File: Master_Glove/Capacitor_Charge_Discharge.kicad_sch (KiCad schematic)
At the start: 0 parts

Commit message: Switch+555+SR
work in progress
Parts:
- added C1: 10u, symbol Device:C
- added R8: 68k, symbol Device:R
- added SW1: SW_Push, symbol Switch:SW_Push
- added U3: MIC1551YM5-TR, Package_TO_SOT_SMD:SOT-23-5, symbol Battery_Management:MCP73811T-435I-OT
- added U4: TC7WH02FU, symbol 74xGxx:74AUC2G02
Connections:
- new net: C1.1, R8.2, U3.5 (TRG)
- new net: SW1.2, U3.4 (TRG)
- new net: U4.5, U4.7
- new net +5V: SW1.1, U3.1 (VS), U4.8 (VCC)
- new net 1Hz: R8.1, U3.3 (OUT), U4.1
- new net GND: C1.2, U3.2 (GND), U4.4 (GND)
- new net Reset: U4.6
- new net SR_Output: U4.2, U4.3
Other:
- note added: "1Hz generator with pushbutton"
- note added: "Reset"
- note added: "Set"
- note added: "Set-Reset circuit"
- note added: "f = 1 / ( k1*R*C ) k1 = 1.44"

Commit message: work on discharge
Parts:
- added C2: 18nF, symbol Device:C
- added C3, C4: 100nF, symbol Device:C
- added R9: 1k, symbol Device:R
- added U5: 74LVC1G08, symbol 74xGxx:74LVC1G08
- added U6: 74AHC1G14, symbol 74xGxx:74AHC1G14
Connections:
- net +5V: now also C3.1, C4.1, U6.5 (VCC)
- net GND: now also C2.2, C3.2, C4.2, U6.3 (GND)
- new net: C2.1, R9.2, U6.2
- new net 40KHz: R9.1, U6.4
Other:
- note added: "Enable?"
- note added: "Exemple A retravailler..."
- note added: "Schmitt oscillator circuit"

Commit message: Working on emitter Circuit
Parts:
- removed U5: 74LVC1G08, symbol 74xGxx:74LVC1G08
- added C7: 100nF, symbol Device:C
- added U5: MIC1551YM5-TR, Package_TO_SOT_SMD:SOT-23-5, symbol Battery_Management:MCP73811T-435I-OT
- added U7: TC7WH02FU, symbol 74xGxx:74AUC2G02
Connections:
- net +5V: now also C7.1, U7.8 (VCC)
- net 40KHz: now also U7.2
- net GND: now also C7.2, U7.4 (GND)
- net SR-_Output: now reaches U4.5, U4.7
- net SR-_Output: now also U7.1
- new net 555_En_pin: U7.7
- no-connect marks 0 -> 3
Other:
- note added: "555 circuit connected to sensor"
- note removed: "Enable?"
- note removed: "Exemple A retravailler..."

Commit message: Circuit ready for review
Added connection to sensor with push-pull output circuit and changed resistances to be U.S.A. format
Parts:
- removed unit 3 of U4
- removed U5: MIC1551YM5-TR, Package_TO_SOT_SMD:SOT-23-5, symbol Battery_Management:MCP73811T-435I-OT
- removed unit 3 of U7
- added C17: 100nF, symbol Device:C
- added Q1: NPN, symbol Simulation_SPICE:NPN
- added Q2: PNP, symbol Simulation_SPICE:PNP
- added Q3: PUMD3, Package_TO_SOT_SMD:SOT-363_SC-70-6, symbol Transistor_BJT:PUMT1
- R8, R9: symbol Device:R -> Device:R_US
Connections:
- net +5V: now also C17.1, Q1.1 (C), Q3.4 (E2)
- net 555_En_pin: now also Q3.2 (B1), Q3.5 (B2)
- net GND: now also C17.2, Q2.3 (E), Q3.1 (E1)
- new net OPA2340_U2B_PIN6: Q1.3 (E), Q2.1 (C), Q3.3 (C2), Q3.6 (C1)
- new net OPA2340_U2B_PIN7: Q1.2 (B), Q2.2 (B)
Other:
- note added: "*Replaced 555 with Pushpull circuit Push-pull using PUMD3 (cheapest NPN/PNP on digikey)"
- note added: "+"
- note added: "-"
- note added: "Amp"
- note added: "Classic Push-Pull output Whats the Amp for?"
- note removed: "555 circuit connected to sensor"
- moved on the sheet: C4, C7

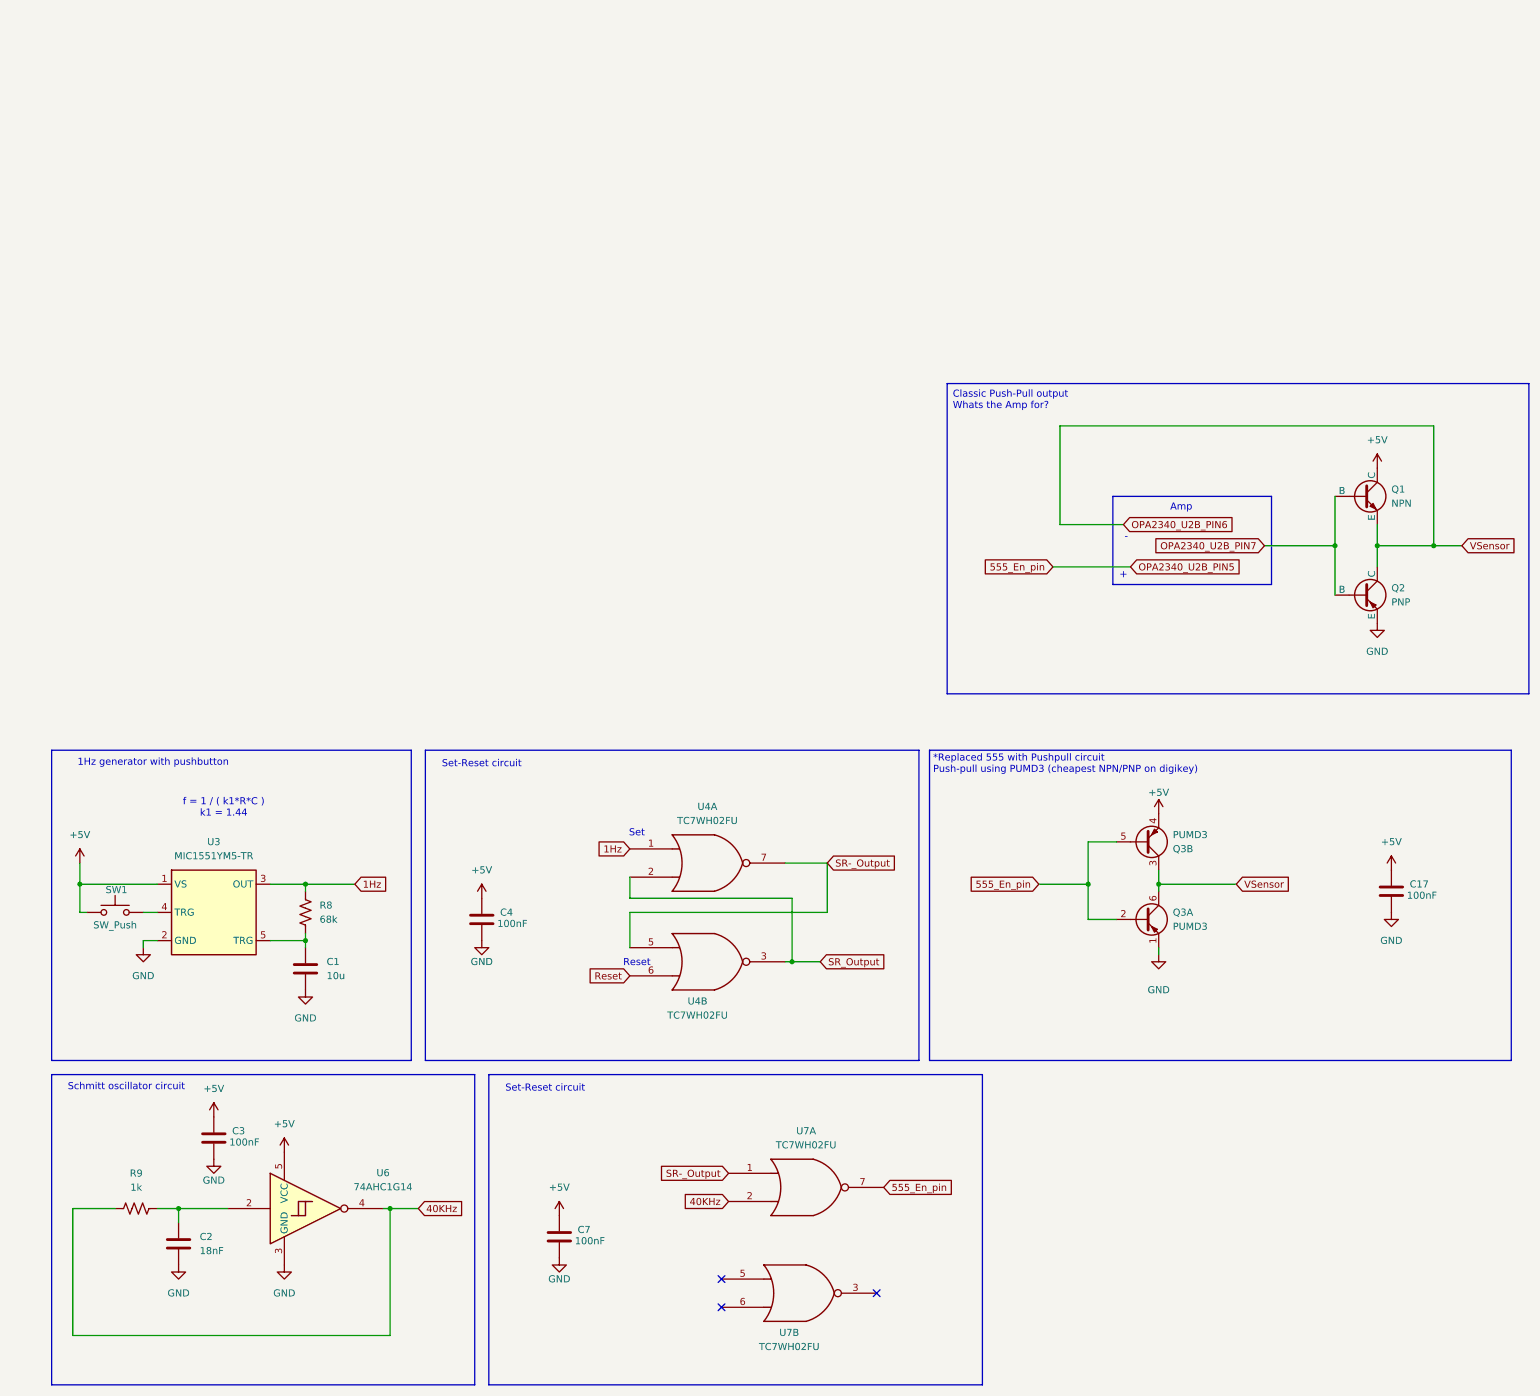
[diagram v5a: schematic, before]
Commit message: Simplifications and modifications following Myriam Recommendation
Circuit will be validated this weekend by Myriam
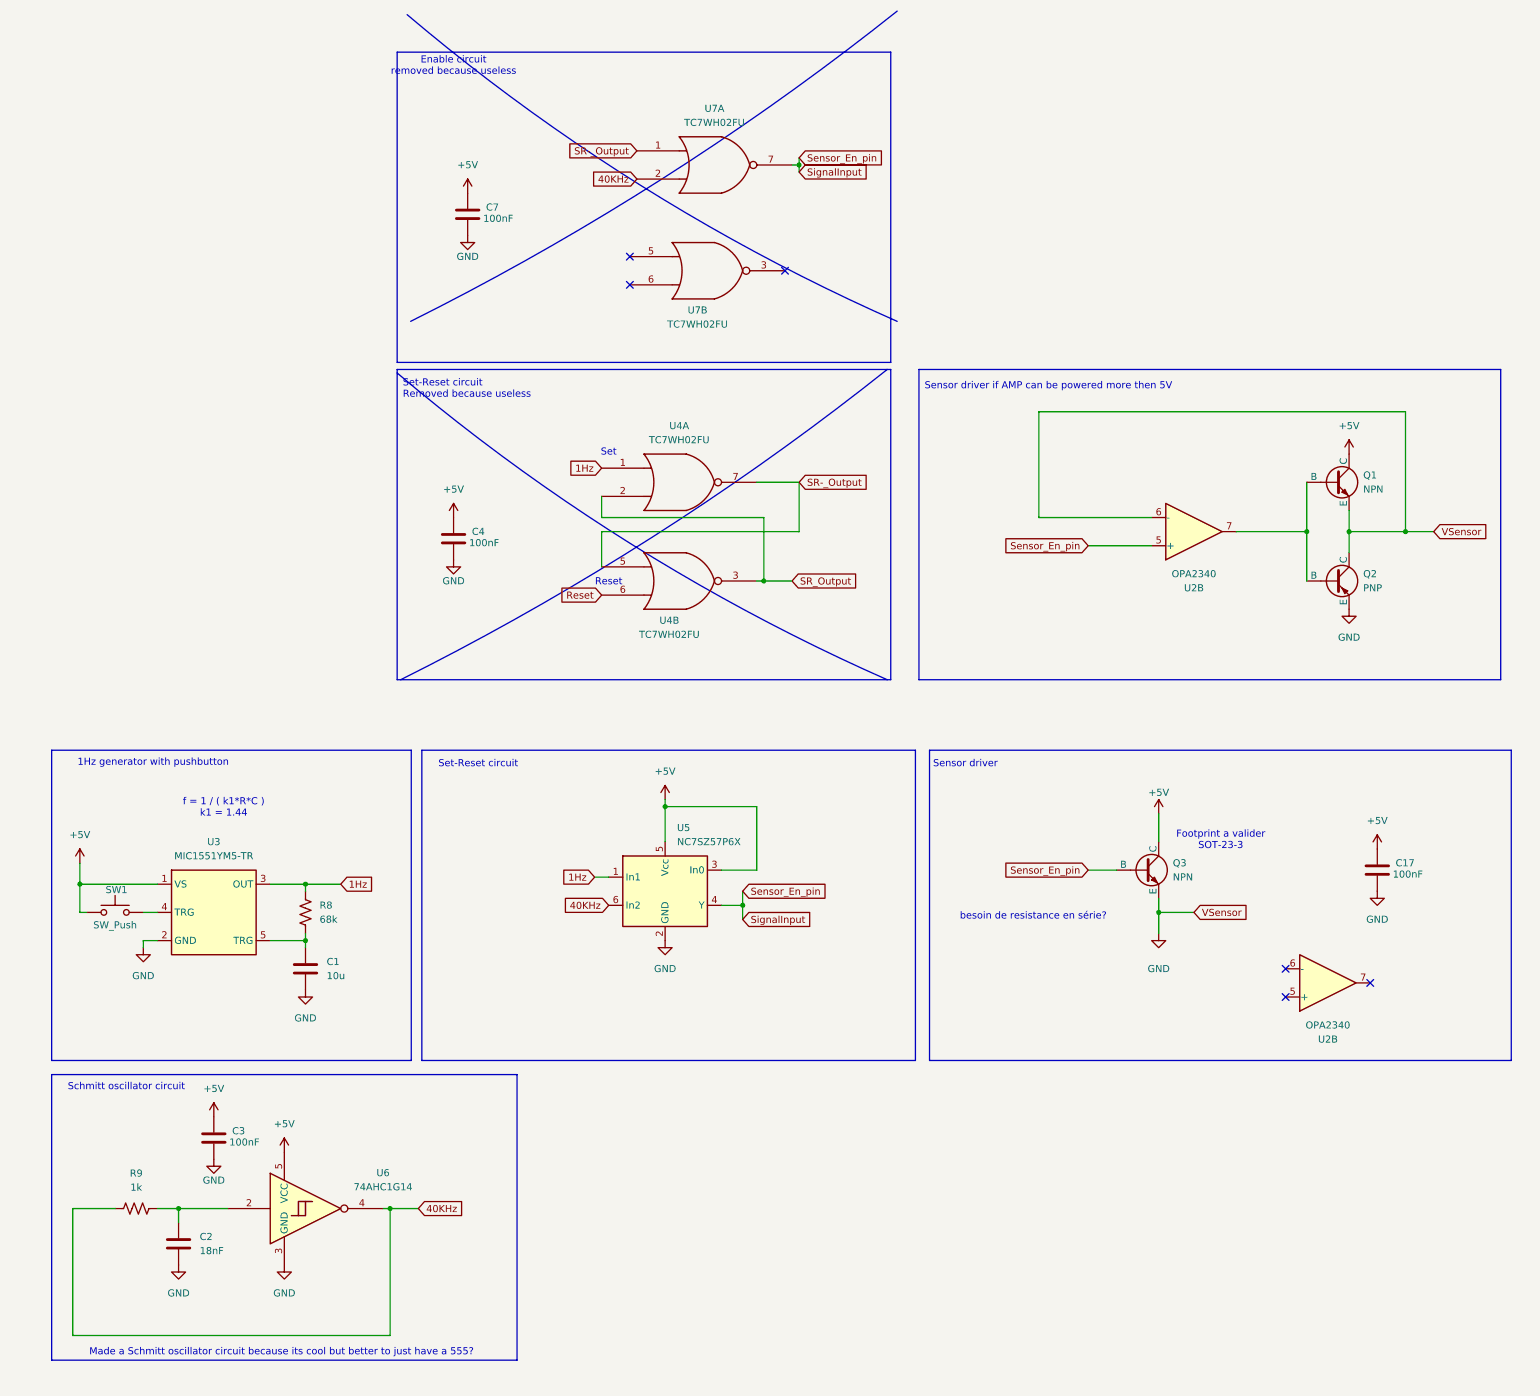
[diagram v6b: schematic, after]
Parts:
- removed Q3: PUMD3, Package_TO_SOT_SMD:SOT-363_SC-70-6, symbol Transistor_BJT:PUMT1
- added Q3: NPN, symbol Simulation_SPICE:NPN
- added U2 (x2): OPA2340, symbol Amplifier_Operational:OPA2340
- added U5: NC7SZ57P6X, Package_TO_SOT_SMD:SOT-363_SC-70-6, symbol Components_Lib:NC7SZ57P6X
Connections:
- net OPA2340_U2B_PIN6 is gone; now on net GND: Q1.3 (E), Q2.1 (C)
- net +5V: now also Q3.1 (C), U5.3 (In0), U5.5 (Vcc)
- net 1Hz: now also U5.1 (In1)
- net 40KHz: now also U5.6 (In2)
- net GND: now also Q3.3 (E), U2.6 (-), U5.2 (GND)
- net 555_En_pin renamed Sensor_En_pin
- net Sensor_En_pin: now also Q3.2 (B), U2.5 (+), U5.4 (Y)
- net OPA2340_U2B_PIN7: no longer names the net of Q1.2 (B), Q2.2 (B)
- net OPA2340_U2B_PIN7: now also U2.7
- no-connect marks 3 -> 6
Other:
- note added: "Enable circuit removed because useless"
- note added: "Footprint a valider SOT-23-3"
- note added: "Made a Schmitt oscillator circuit because its cool but better to just have a 555?"
- note added: "Sensor driver"
- note added: "Sensor driver if AMP can be powered more then 5V"
- note added: "Set-Reset circuit Removed because useless"
- note added: "besoin de resistance en série?"
- note removed: "*Replaced 555 with Pushpull circuit Push-pull using PUMD3 (cheapest NPN/PNP on digikey)"
- note removed: "+"
- note removed: "-"
- note removed: "Amp"
- note removed: "Classic Push-Pull output Whats the Amp for?"
- moved on the sheet: C17, C4, C7, Q1, Q2, U4A, U4B, U7A, U7B

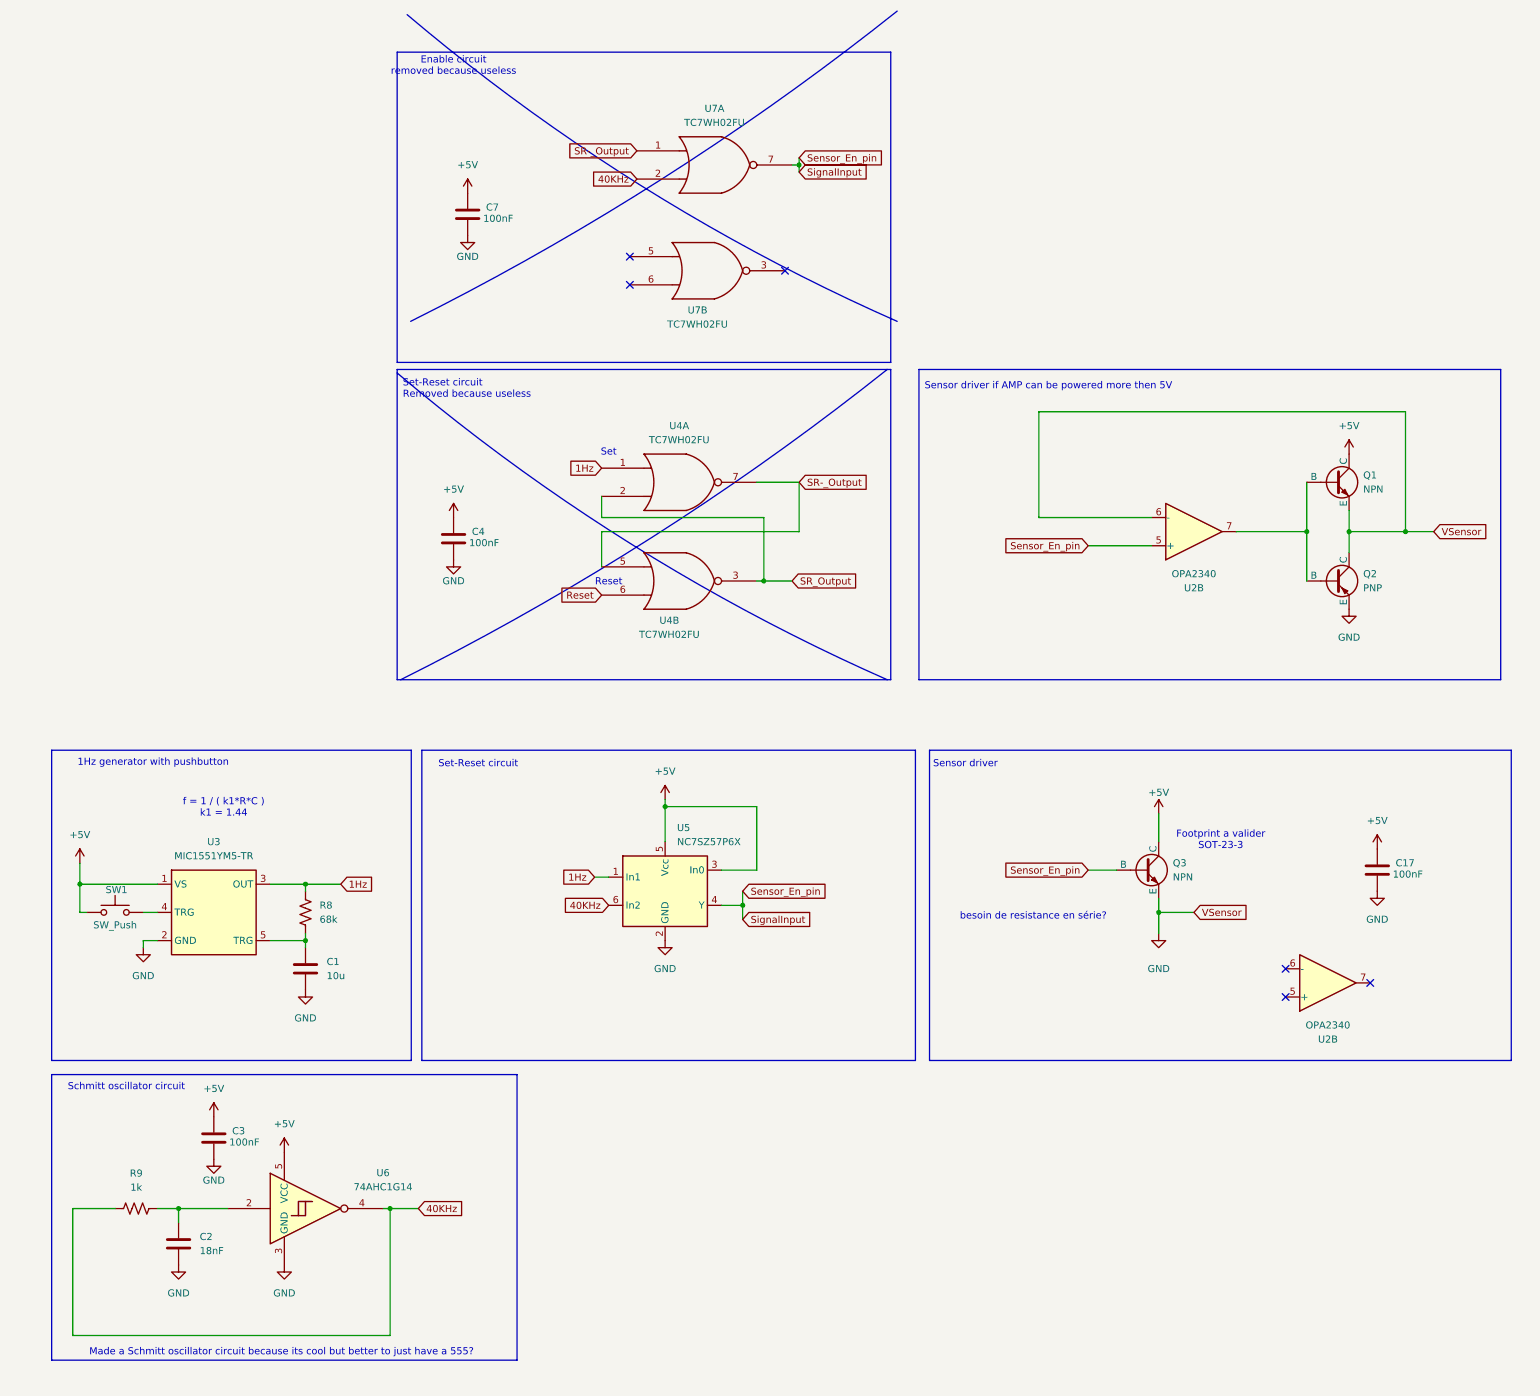
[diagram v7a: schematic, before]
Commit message: Modifications according to reccomendation
Changed Vcc to +5V
Subbed MIC1551 to MIC 1553
Added debounce on button
Fixed other small bugs
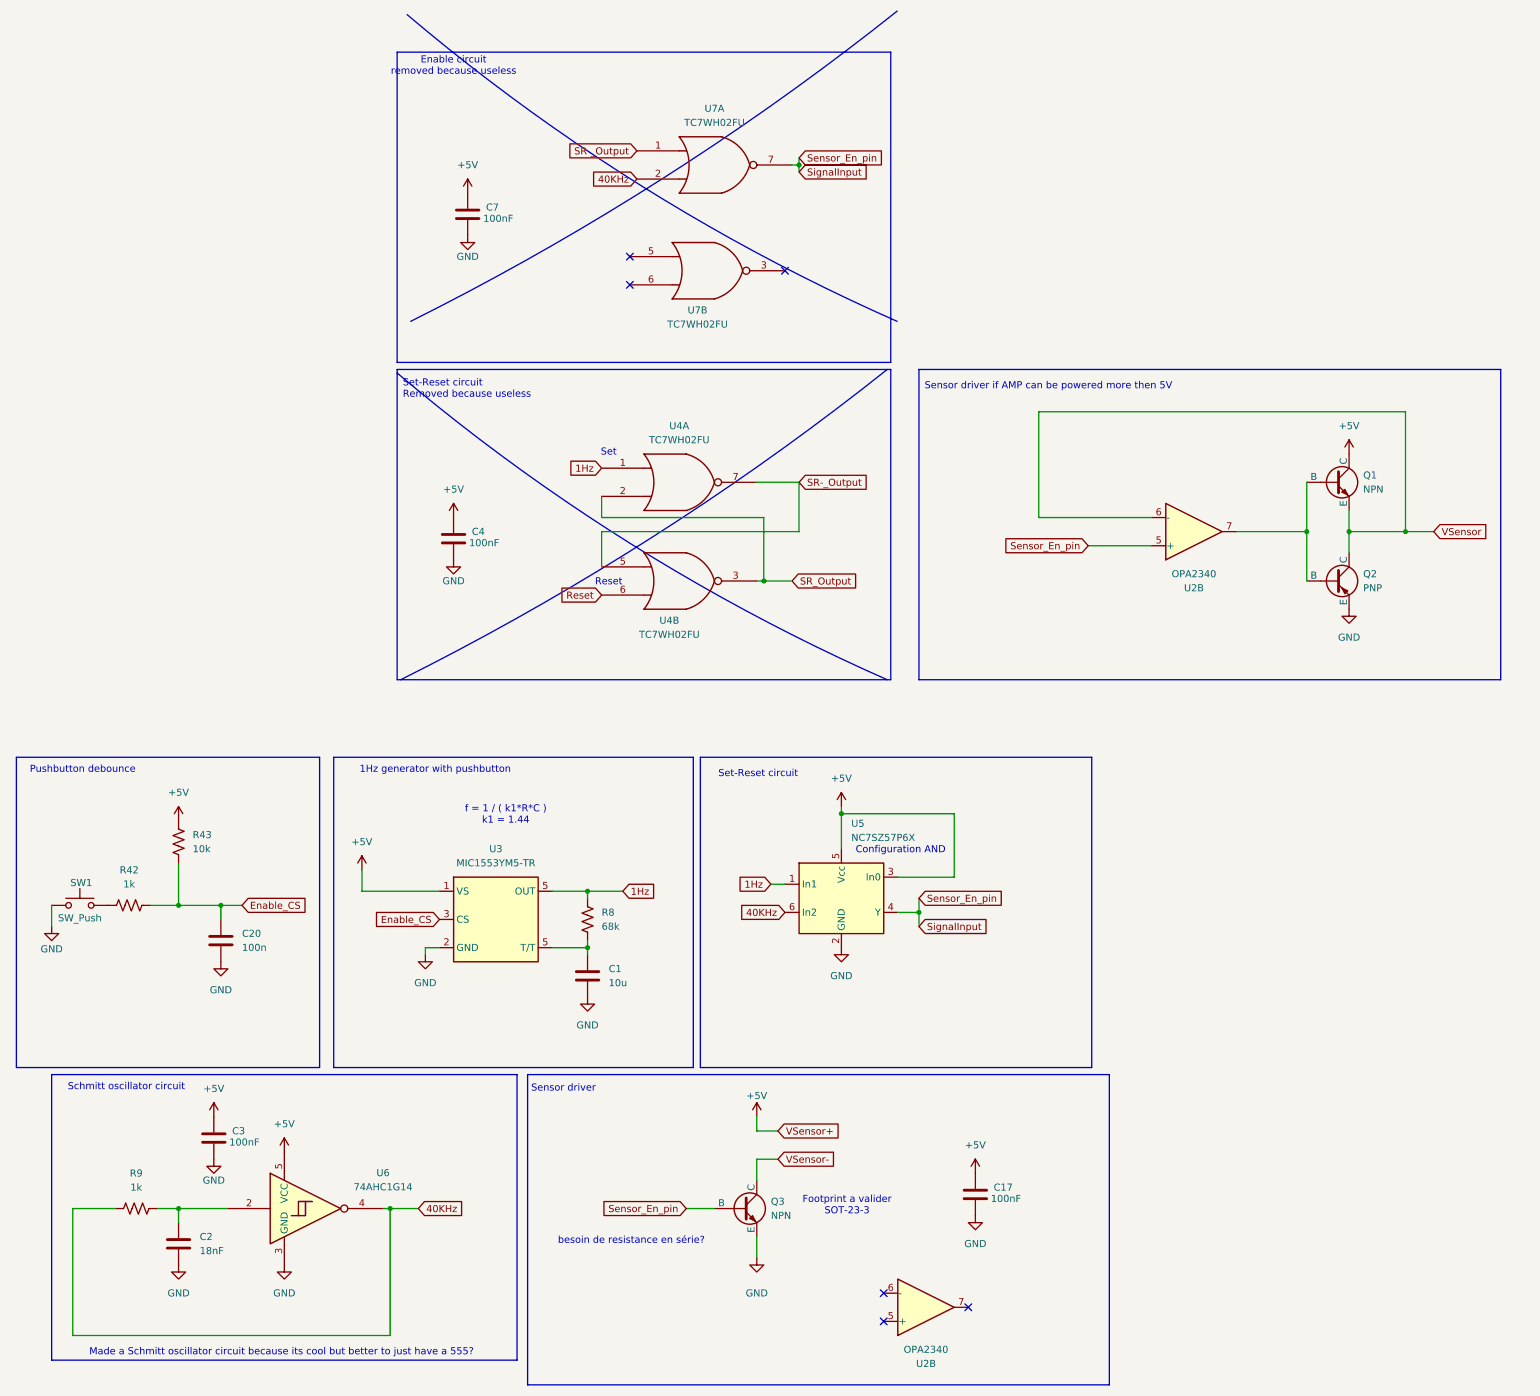
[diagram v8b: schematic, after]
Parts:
- added C20: 100n, symbol Device:C
- added R42: 1k, symbol Device:R_US
- added R43: 10k, symbol Device:R_US
- U3: value MIC1551YM5-TR -> MIC1553YM5-TR
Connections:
- net +5V: now also R43.2; no longer Q3.1 (C), SW1.1
- net 1Hz: now also U3.5 (T/T); no longer U3.3 (OUT)
- net GND: now also SW1.1, C20.2; no longer Q1.3 (E), Q2.1 (C), U2.6 (-)
- net at SW1.2: now also R42.1; no longer U3.4 (TRG)
- new net Enable_CS: C20.1, R42.2, R43.1, U3.3 (CS)
- new net VSensor: Q1.3 (E), Q2.1 (C), U2.6 (-)
- new net VSensor-: Q3.1 (C)
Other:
- note added: "Configuration AND"
- note added: "Pushbutton debounce"
- moved on the sheet: C1, C17, Q3, R8, SW1, U2B, U3, U5
